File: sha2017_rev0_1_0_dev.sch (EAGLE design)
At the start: 201 parts, among them IC1 CP210X_USB_UART, IC2 AP7215, IC3 ESP32WROOM32, IC4 MCP73833, IC5 FXL6408, IC6 CPT112, Q2 MMBT2222A, Q3 MMBT2222A, Q4 MMBT2222A, Q5 MMBT2222A, Q6 SI1304 BDL, Q7 MMBT2222A, T1 SI2301DS, T2 SI2301DS, T3 SI2301DS, X1 2908-05WB-MG, X3 JST-PH3

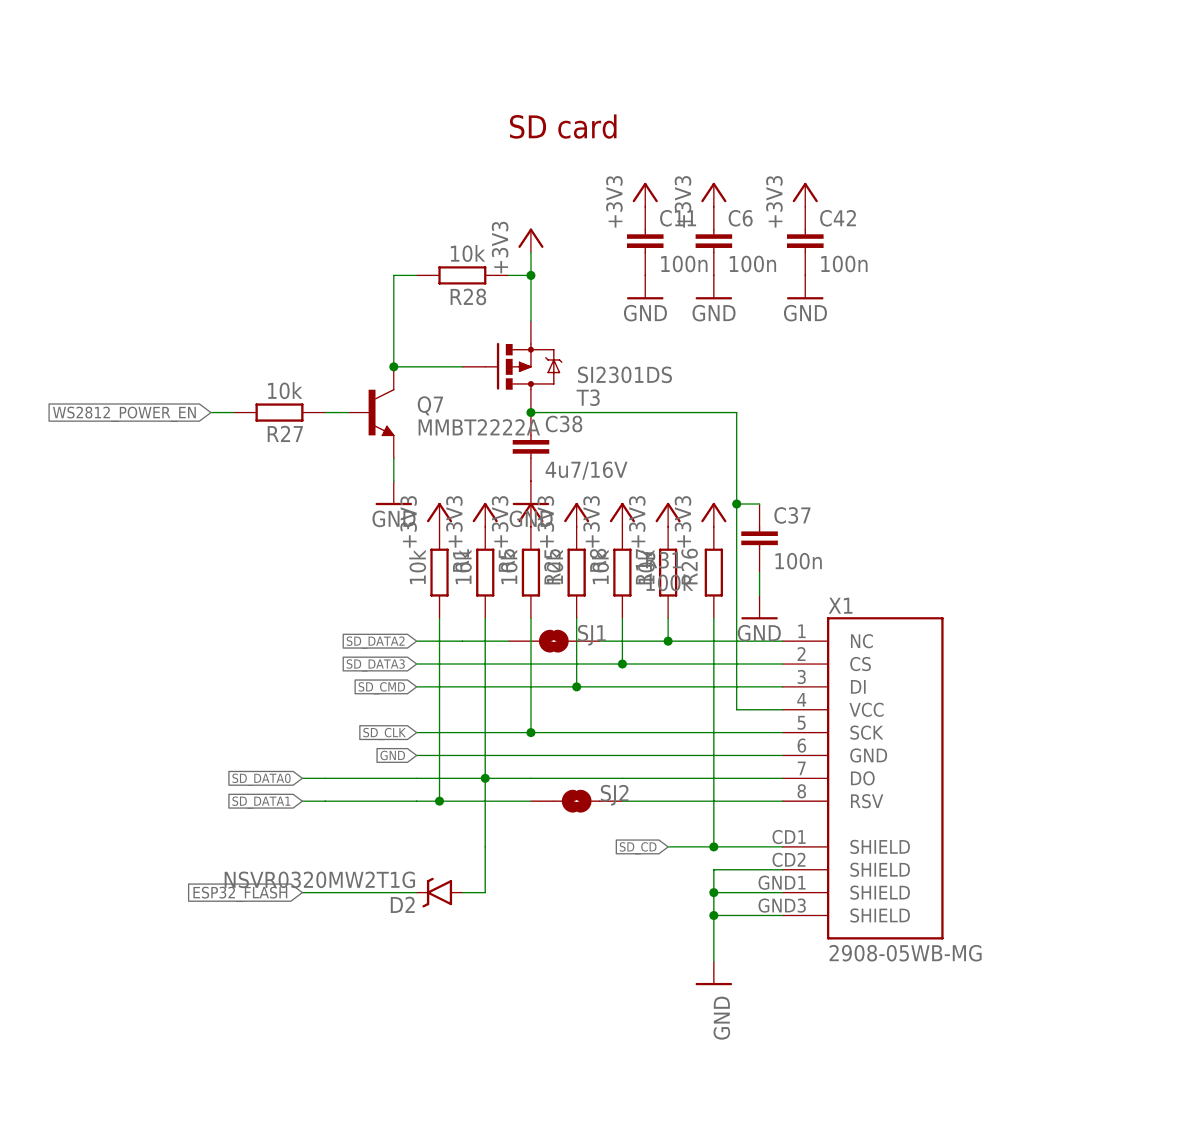
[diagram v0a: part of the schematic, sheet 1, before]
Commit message: SD pullups to 3V3_SWITCHED
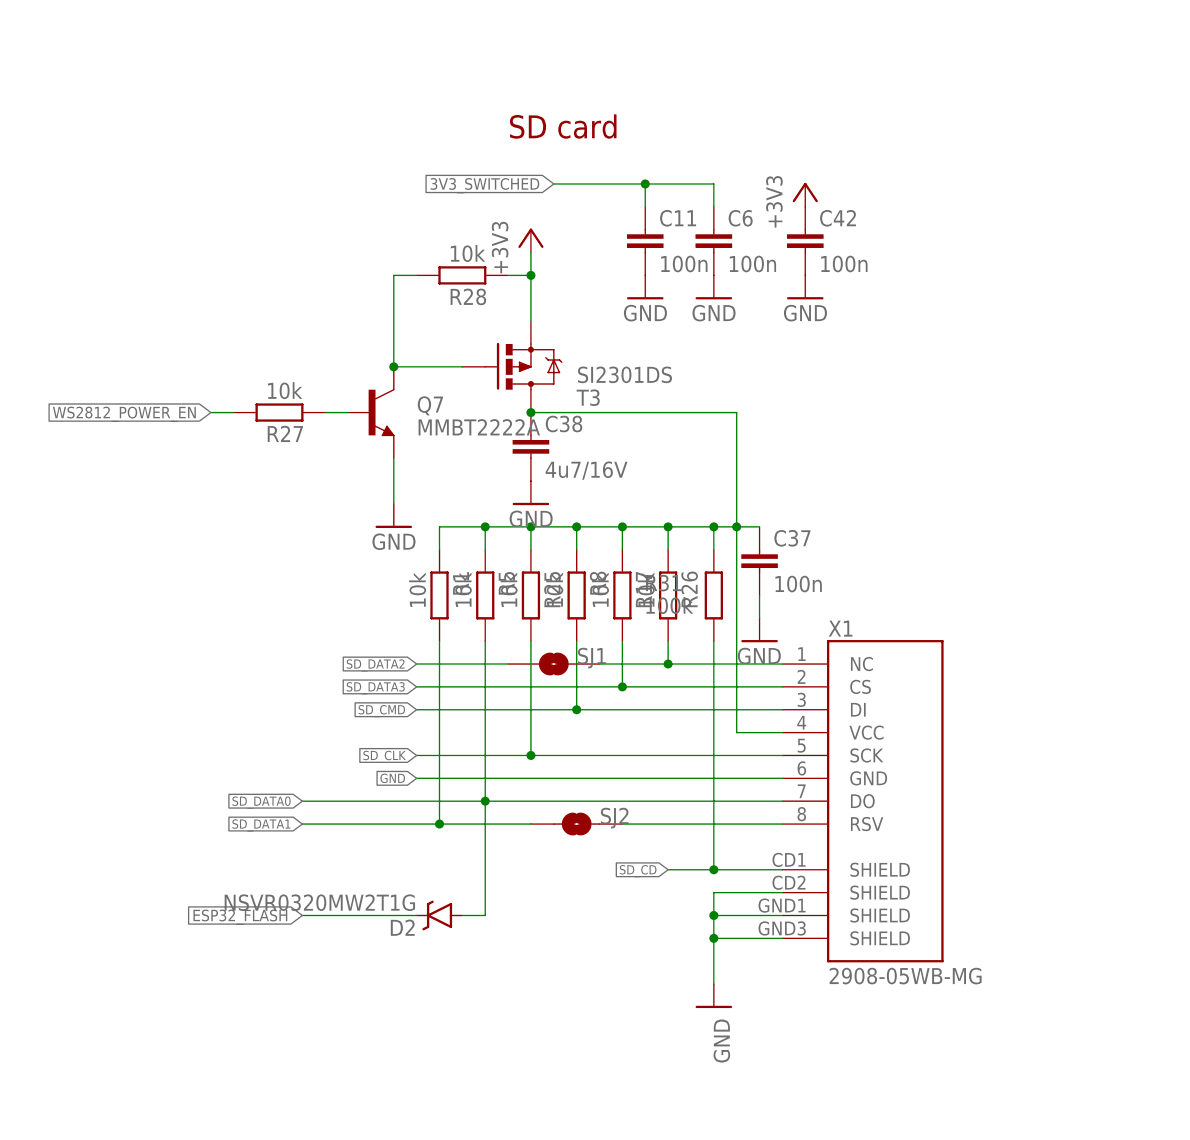
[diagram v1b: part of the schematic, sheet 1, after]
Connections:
- net +3V3: no longer C11.1, C6.1, R1.2, R17.2, R25.2, R26.2, R31.1, R5.2, R8.2
- net 3V3_SWITCHED: now also C11.1, C6.1, R1.2, R17.2, R25.2, R26.2, R31.1, R5.2, R8.2
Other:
- moved on the sheet: C37, D2, R1, R17, R25, R26, R31, R5, R8, SJ1, SJ2, X1

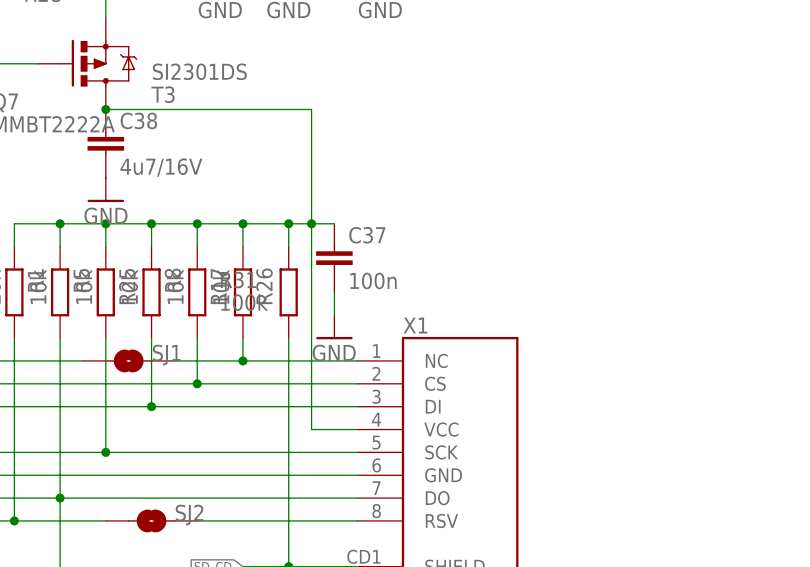
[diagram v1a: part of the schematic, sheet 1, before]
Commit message: fixing broken ground plane
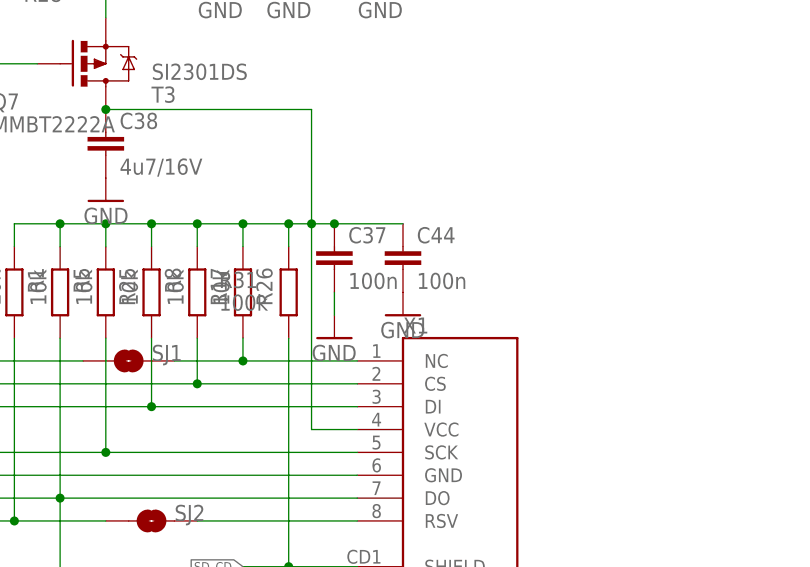
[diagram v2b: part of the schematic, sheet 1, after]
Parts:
- added C44: 100n, sha2017_rev0_1_0_dev:C0603-DASHES
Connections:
- net 3V3_SWITCHED: now also C44.1
- net GND: now also C44.2
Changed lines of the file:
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@@
 </part>
 <part name="GND96" library="supply1" deviceset="GND" device=""/>
+<part name="C44" library="sha2017_rev0_1_0_dev" deviceset="C0603-DASHES" device="" value="100n">
+<attribute name="PARTNO" value="GRM188R71H104KA93D"/>
+</part>
+<part name="GND97" library="supply1" deviceset="GND" device=""/>
 </parts>
 <sheets>
@@
 <attribute name="PARTNO" x="144.78" y="40.64" size="1.778" layer="96" display="off"/>
 </instance>
+<instance part="C44" gate="G$1" x="172.72" y="69.85">
+<attribute name="PARTNO" x="172.72" y="69.85" size="1.778" layer="96" rot="MR0" display="off"/>
+</instance>
+<instance part="GND97" gate="1" x="172.72" y="63.5"/>
 </instances>
 <busses>
@@
 <pinref part="C38" gate="G$1" pin="2"/>
 <pinref part="GND57" gate="1" pin="GND"/>
+</segment>
+<segment>
+<pinref part="C44" gate="G$1" pin="2"/>
+<pinref part="GND97" gate="1" pin="GND"/>
 </segment>
 </net>
@@
 <junction x="154.94" y="73.66"/>
 <junction x="160.02" y="73.66"/>
-</segment>
-<segment>
+<pinref part="C44" gate="G$1" pin="1"/>
+<wire x1="165.1" y1="73.66" x2="172.72" y2="73.66" width="0.1524" layer="91"/>
+<junction x="165.1" y="73.66"/>
+</segment>
+<segment>

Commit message: add some color
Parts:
- removed Q7: MMBT2222A, SparkFun-DiscreteSemi:TRANSISTOR_NPNMMBT2222A
- removed TP5: TEST-POINT3, SparkFun-Passives:TEST-POINT3
- removed U$23, U$24, U$25: VIA, badge:VIA
- added $$U$4, $$U$5, $$U$6: VIA, badge:VIA
- added Q1: MMBT2222A, SparkFun-DiscreteSemi:TRANSISTOR_NPNMMBT2222A
- added TP140: TEST-POINT3, SparkFun-Passives:TEST-POINT3
- C10, C42: OC_FARNELL (none) -> unknown
- C13, C26, C41: value 100n -> 4u7/16V; device sha2017_rev0_1_0_dev:C0603-DASHES -> rcl:C-EUC0805; PARTNO GRM188R71H104KA93D -> GRM21BR61C475KA88K
- C14, C22, C4, C8: value 4u7/16V -> 100n; device rcl:C-EUC0805 -> sha2017_rev0_1_0_dev:C0603-DASHES; PARTNO GRM21BR61C475KA88K -> GRM188R71H104KA93D
- C15, C9: value 100n -> 4u7/16V; device sha2017_rev0_1_0_dev:C0603-DASHES -> rcl:C-EUC0805; OC_FARNELL unknown -> (none); PARTNO GRM188R71H104KA93D -> GRM21BR61C475KA88K
- C16, C29: value 4u7/16V -> 100n; device rcl:C-EUC0805 -> sha2017_rev0_1_0_dev:C0603-DASHES; OC_FARNELL (none) -> unknown; PARTNO GRM21BR61C475KA88K -> GRM188R71H104KA93D
- C18, C20, C24, C30, C34: value 1u -> 4u7/16V; device sha2017_rev0_1_0_dev:C0603-DASHES -> rcl:C-EUC0805; PARTNO GRM188R61E105KA12D -> GRM21BR61C475KA88K
- C19, C25, C32, C38: value 4u7/16V -> 1u; device rcl:C-EUC0805 -> sha2017_rev0_1_0_dev:C0603-DASHES; PARTNO GRM21BR61C475KA88K -> GRM188R61E105KA12D
- C21: value 100n -> 1u; PARTNO GRM188R71H104KA93D -> GRM188R61E105KA12D
- C27: OC_FARNELL unknown -> (none)
- C31: value 1u -> 100n; PARTNO GRM188R61E105KA12D -> GRM188R71H104KA93D
- C39: value 100n -> 1u; OC_FARNELL unknown -> (none); PARTNO GRM188R71H104KA93D -> GRM188R61E105KA12D
- Q5: value MMBT2222A -> SI1304 BDL; device SparkFun-DiscreteSemi:TRANSISTOR_NPNMMBT2222A -> SparkFun-DiscreteSemi:MOSFET-NCHANNEL2N7002PW; PARTNO BC817-25,215 -> SI1308EDL-T1-GE3
- Q6: value SI1304 BDL -> MMBT2222A; device SparkFun-DiscreteSemi:MOSFET-NCHANNEL2N7002PW -> SparkFun-DiscreteSemi:TRANSISTOR_NPNMMBT2222A; PARTNO SI1308EDL-T1-GE3 -> BC817-25,215
- X1: value 2908-05WB-MG -> (none); device con-3m:2908-05WB-MG -> EAGLE-FPC_CONNECTOR_AND_FFC_CAB-rev1:68712414022; PARTNO 2908-05WB-MG -> 68712414022
- X2: value (none) -> 2908-05WB-MG; device EAGLE-BOARD-TO-BOARD_CONNECTORS-rev16c:610X12243021 -> con-3m:2908-05WB-MG; PARTNO (none) -> 2908-05WB-MG
- X3: value JST-PH3 -> (none); device badge:JST-PH3 -> EAGLE-BOARD-TO-BOARD_CONNECTORS-rev16c:610X12243021
- X4: value (none) -> JST-PH3; device EAGLE-FPC_CONNECTOR_AND_FFC_CAB-rev1:68712414022 -> badge:JST-PH3; PARTNO 68712414022 -> (none)
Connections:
- net +3V3: now also C17.1, C20.1, C22.1, C27.1, C30.1, C37.1, C44.1, TP119.1, X1.10, X1.7, X1.9; no longer C16.1, C19.1, C21.1, C25.1, C29.1, C36.1, C40.1, TP118.1, X4.10, X4.7, X4.9
- net +5V: now also C11.1, C24.1, C9.1, TP112.1; no longer C10.1, C22.1, C8.1, TP111.1
- net 3V3_SWITCHED: now also C12.1, C31.1, C40.1, C41.1, C7.1, TP116.1, X2.VCC, X3.1; no longer C11.1, C37.1, C38.1, C44.1, C6.1, TP115.1, X1.VCC, X2.1
- net CD0: now also TP131.1; no longer TP130.1
- net CLK: now also TP130.1; no longer TP129.1
- net CND: now also TP128.1; no longer TP127.1
- net ESP32_!RESET: now also Q3.C, TP121.1; no longer Q4.C, TP120.1
- net ESP32_FLASH: now also Q4.C, TP120.1; no longer Q5.C, TP119.1
- net EXTIO-0: now also X3.10; no longer X2.10
- net EXTIO-1: now also X3.9; no longer X2.9
- net EXTIO-2: now also X3.8; no longer X2.8
- net EXTIO-3: now also X3.4; no longer X2.4
- net EXTIO-4: now also X3.3; no longer X2.3
- net EXTIO-5: now also X3.2; no longer X2.2
- net GDR: now also Q5.G, TP124.1, X1.23; no longer Q6.G, TP123.1, X4.23
- net GND: now also $$U$4.P$1, $$U$5.P$1, $$U$6.P$1, C12.2, C18.2, C19.1, C20.2, C21.1, C24.2, C27.2, C29.1, C30.2, C31.2, C32.1, C34.2, C36.1, C38.1, C4.1, C41.2, C6.1, Q1.E, Q6.E, TP1.1, TP106.1, TP122.1, TP125.1, TP140.1, X1.17, X1.8, X2.GND, X2.SHIELD@2, X2.SHIELD@3, X2.SHIELD@4, X3.12, X42.1; no longer C12.1, C18.1, C19.2, C20.1, C21.2, C25.2, C27.1, C29.2, C30.1, C31.1, C32.2, C34.1, C36.2, C38.2, C4.2, C41.1, C6.2, Q3.E, Q7.E, TP121.1, TP124.1, TP139.1, TP3.1, TP5.1, U$23.P$1, U$24.P$1, U$25.P$1, X1.GND, X1.SHIELD@2, X1.SHIELD@3, X1.SHIELD@4, X2.12, X32.1, X4.17, X4.8
- net I2C_SCL: now also TP114.1, X3.7; no longer TP113.1, X2.7
- net I2C_SDA: now also TP115.1, X3.6; no longer TP114.1, X2.6
- net LCD_!RESET: now also TP113.1, X1.15; no longer TP112.1, X4.15
- net LCD_BUSY: now also TP118.1, X1.16; no longer TP117.1, X4.16
- net LCD_CS: now also TP109.1, X1.13; no longer TP108.1, X4.13
- net LCD_D/!S: now also TP111.1, X1.14; no longer TP110.1, X4.14
- net LCD_MOSI: now also TP107.1, X1.11; no longer TP106.1, X4.11
- net LCD_SCK: now also TP108.1, X1.12; no longer TP107.1, X4.12
- net N$10: now also Q3.E; no longer Q4.E
- net N$11: now also Q4.E; no longer Q5.E
- net N$13: now also Q4.B; no longer Q5.B
- net N$14: now also Q3.B; no longer Q4.B
- net N$15: now also Q6.B; no longer Q7.B
- net N$16: now also Q2.C; no longer Q3.C
- net N$17: now also Q6.C; no longer Q7.C
- net N$22: now also C25.1; no longer C24.1
- net N$23: now also C25.2, Q5.D; no longer C24.2, Q6.D
- net N$3: now also D104.DOUT; no longer D105.DOUT
- net N$32: now also TP139.1; no longer TP136.1
- net N$4: now also D104.DIN, D105.DOUT; no longer D104.DOUT, D105.DIN
- net N$42: now also C28.2; no longer C27.2
- net N$43: now also C29.2; no longer C28.2
- net N$45: now also Q2.B; no longer Q3.B
- net N$48: now also X41.1; no longer X31.1
- net N$49: now also C34.1, X43.1; no longer C32.1, X33.1
- net N$52: now also Q1.B; no longer Q2.B
- net N$53: now also Q1.C; no longer Q2.C
- net N$6: now also X2.RSV; no longer X1.RSV
- net N$61: now also TP3.1; no longer TP2.1
- net N$62: now also TP2.1; no longer TP1.1
- net PREVGH: now also C32.2, X1.4; no longer C30.2, X4.4
- net PREVGL: now also C36.2, X1.2; no longer C34.2, X4.2
- net RESE: now also Q5.S, TP123.1, X1.22; no longer Q6.S, TP122.1, X4.22
- net SD1: now also TP132.1; no longer TP131.1
- net SD2: now also TP126.1; no longer TP125.1
- net SD3: now also TP127.1; no longer TP126.1
- net SD_CD: now also X2.SHIELD@1; no longer X1.SHIELD@1
- net SD_CLK: now also X2.SCK; no longer X1.SCK
- net SD_CMD: now also X2.DI; no longer X1.DI
- net SD_DATA0: now also X2.DO; no longer X1.DO
- net SD_DATA2_OUT: now also X2.NC; no longer X1.NC
- net SD_DATA3: now also X2.CS; no longer X1.CS
- net TSCL: now also X1.19; no longer X4.19
- net TSDA: now also X1.18; no longer X4.18
- net VBAT: now also TP110.1; no longer TP109.1
- net VBAT_SENSE: now also C16.1; no longer C15.1
- net VCC: now also C15.1, C18.1, TP129.1; no longer C13.1, C17.1, TP128.1
- net VCOM: now also C38.2, X1.1; no longer C35.2, X4.1
- net VDD: now also C8.1; no longer C7.1
- net VGH: now also C21.2, X1.20; no longer C20.2, X4.20
- net VGL: now also C19.2, X1.21; no longer C18.2, X4.21
- net VPP: now also X1.6; no longer X4.6
- net VSH: now also C33.2, X1.5; no longer C31.2, X4.5
- net VSL: now also C35.2, X1.3; no longer C33.2, X4.3
- net VUSB_SENSE: now also C10.1; no longer C9.1
- net WS2812_DATA: now also D105.DIN, TP136.1; no longer D104.DIN, TP132.1
- net WS2812_DATA_OUT: now also X3.5; no longer X2.5
- net WS2812_POWER: now also C13.1, C4.2, C6.2, TP117.1, X3.11; no longer C12.2, C4.1, C41.2, TP116.1, X2.11
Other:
- moved on the sheet: C1, C11, C14, C15, C16, C17, C19, C20, C22, C26, C28, C3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

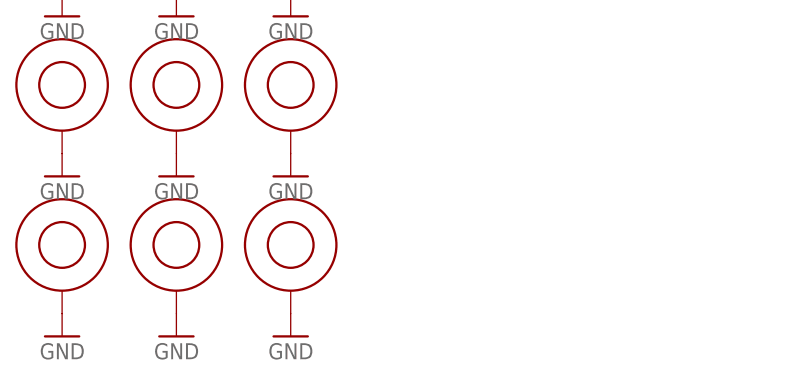
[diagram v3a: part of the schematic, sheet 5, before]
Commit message: add missin ground via at cpt112 programming interface
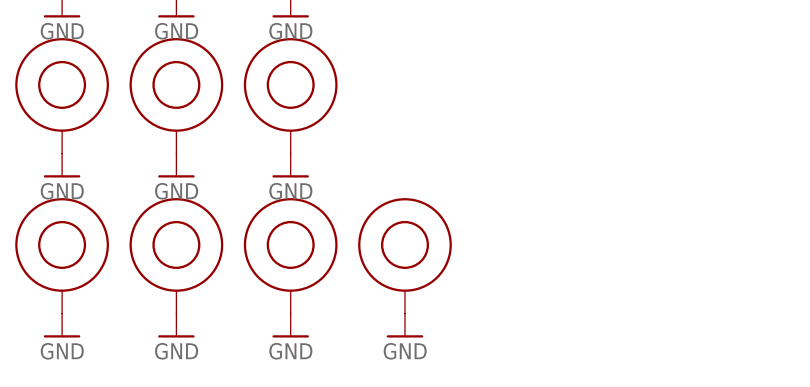
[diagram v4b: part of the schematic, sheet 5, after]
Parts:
- added U$23: VIA, badge:VIA
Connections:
- net GND: now also U$23.P$1
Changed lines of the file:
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@@
 </part>
 <part name="GND97" library="supply1" deviceset="GND" device=""/>
+<part name="U$23" library="badge" deviceset="VIA" device="">
+<attribute name="PARTNO" value="NAP"/>
+</part>
+<part name="GND98" library="supply1" deviceset="GND" device=""/>
 </parts>
 <sheets>
@@
 </instance>
 <instance part="GND96" gate="1" x="83.82" y="139.7"/>
+<instance part="U$23" gate="G$1" x="83.82" y="27.94">
+<attribute name="PARTNO" x="83.82" y="27.94" size="5.08" layer="96" display="off"/>
+</instance>
+<instance part="GND98" gate="1" x="83.82" y="17.78" rot="MR0"/>
 </instances>
 <busses>
@@
 <pinref part="GND96" gate="1" pin="GND"/>
 </segment>
+<segment>
+<pinref part="U$23" gate="G$1" pin="P$1"/>
+<pinref part="GND98" gate="1" pin="GND"/>
+</segment>
 </net>

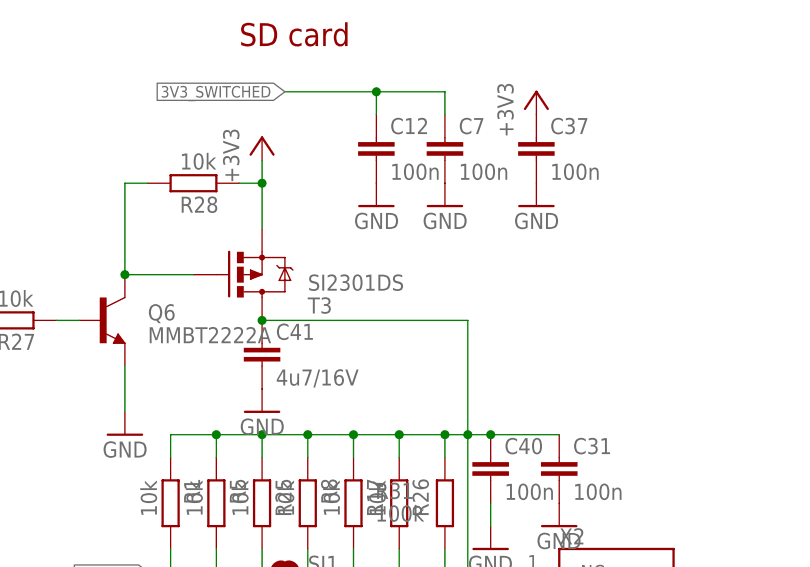
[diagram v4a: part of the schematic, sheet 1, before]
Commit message: fixed some values
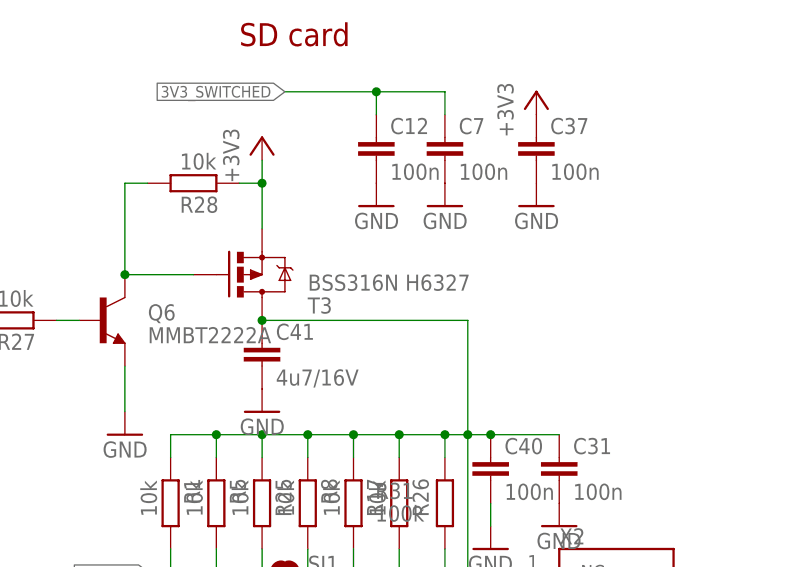
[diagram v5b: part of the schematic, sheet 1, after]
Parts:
- IC4: PARTNO (none) -> MCP73833-BZI/UN
- IC5: PARTNO (none) -> FXL6408UMX
- IC6: PARTNO (none) -> CPT112S-A02-GM
- R2: PARTNO (none) -> ERJ-3GEYJ220V
- R20, R31, R6: PARTNO CRCW0603100KFKEA -> ERJ-3GEYJ104V
- R21, R7: PARTNO (none) -> ERJ-3GEYJ224V
- R29: PARTNO (none) -> ERJ-3GEYJ222V
- R32: PARTNO (none) -> ERJ-3GEYJ154V
- S1, S2: PARTNO (none) -> SKQGABE010
- T1, T2, T3: value SI2301DS -> BSS316N H6327; PARTNO (none) -> 726-BSS316NH6327XT
- USB1: PARTNO 10118194-0001LF -> 10118192-0001LF
- X3: PARTNO (none) -> 517-153208-2020-TB
